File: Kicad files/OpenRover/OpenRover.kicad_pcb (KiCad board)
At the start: 2 copper layers, 0 parts

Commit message: Updated with Allan his work.
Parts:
- added D1: BAV23, Package_TO_SOT_SMD:SOT-23, F.Cu at (128.0, 64.0)
- added D2: BAV23, Package_TO_SOT_SMD:SOT-23, F.Cu at (139.0, 71.0)
- added D3: BAV23, Package_TO_SOT_SMD:SOT-23, F.Cu at (130.0, 56.0)
- added D4: BAV23, Package_TO_SOT_SMD:SOT-23, F.Cu at (135.0, 56.0)
- added D5: BAV23, Package_TO_SOT_SMD:SOT-23, F.Cu at (135.0, 62.0)
- added D6: BAV23, Package_TO_SOT_SMD:SOT-23, F.Cu at (134.0, 68.0)
- added D7: BAV23, Package_TO_SOT_SMD:SOT-23, F.Cu at (134.0, 74.0)
- added D8: 1N4148W, Diode_SMD:D_SOD-123, F.Cu at (157.0, 76.0)
- added D9: 1N4148W, Diode_SMD:D_SOD-123, F.Cu at (157.0, 71.0)
- added Q1: FQT7N10L, Package_TO_SOT_SMD:SOT-23, F.Cu at (143.0, 58.0)
- added Q2: BC846, Package_TO_SOT_SMD:SOT-23, F.Cu at (128.0, 70.0)
- added Q3: MMDT3906, Package_TO_SOT_SMD:SOT-363_SC-70-6, F.Cu at (127.0, 75.0)
- added U2: MAX4162, Package_TO_SOT_SMD:SOT-23-5, F.Cu at (149.0, 59.0)
- added U4: MAX6008AEUR+T, Package_TO_SOT_SMD:SOT-23, F.Cu at (147.0, 65.0)
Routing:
- net GND: track 0.00 -> 53.6 mm
- net Net-(C4-Pad2): track 0.00 -> 23.5 mm
- net Net-(C2-Pad2): track 0.00 -> 13.1 mm
- net Net-(Q2-Pad1): track 0.00 -> 6.59 mm
- net Net-(C6-Pad2): track 0.00 -> 5.79 mm
- net Net-(R6-Pad2): track 0.00 -> 4.85 mm
- net Net-(C10-Pad2): track 0.00 -> 4.51 mm
- net Net-(C12-Pad2): track 0.00 -> 4.10 mm
- net Net-(C10-Pad1): track 0.00 -> 4.10 mm
- net Net-(Q3-Pad1): track 0.00 -> 2.85 mm
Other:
- board outline added: 54.4 x 34.1 mm

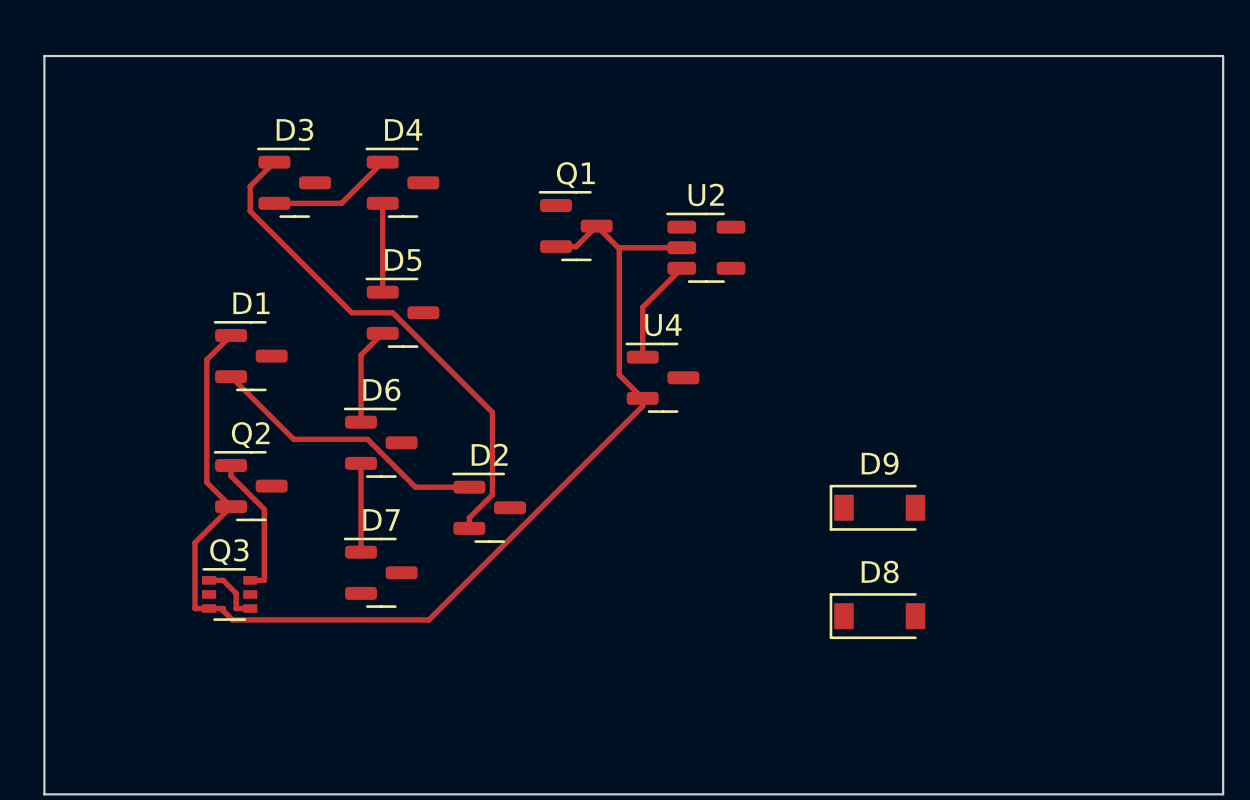
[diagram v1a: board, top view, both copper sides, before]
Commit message: Tested 74HC14 adding to the footprints
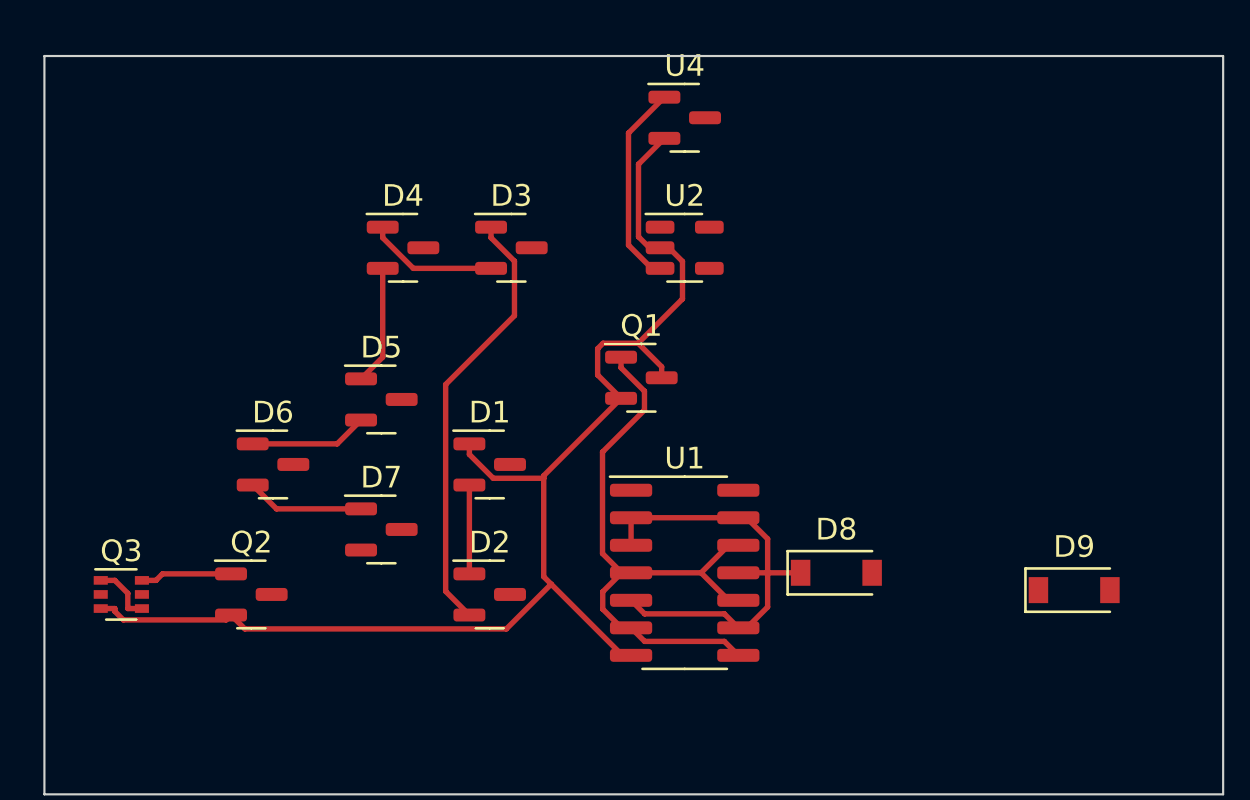
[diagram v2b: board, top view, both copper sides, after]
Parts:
- added U1: 74HC14, Package_SO:SOIC-14_3.9x8.7mm_P1.27mm, F.Cu at (148.0, 74.0)
- moved D1 12.1 mm to (139.0, 69.0)
- moved U4 12.0 mm to (148.0, 53.0)
- moved D3 10.4 mm to (140.0, 59.0)
- moved D9 9.75 mm to (166.0, 74.8)
- moved Q1 7.62 mm to (146.0, 65.0)
- moved D6 5.10 mm to (129.0, 69.0)
- moved Q2 5.00 mm to (128.0, 75.0)
- moved Q3 5.00 mm to (122.0, 75.0)
- moved D5 4.12 mm to (134.0, 66.0)
- moved D2 4.00 mm to (139.0, 75.0)
- moved D4 3.00 mm to (135.0, 59.0)
- moved D8 2.83 mm to (155.0, 74.0)
- moved D7 2.00 mm to (134.0, 72.0)
- moved U2 1.00 mm to (148.0, 59.0)
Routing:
- net Net-(Q1-Pad1): track 0.00 -> 28.9 mm
- net Net-(D8-Pad1): track 0.00 -> 21.2 mm
- net Net-(C2-Pad2): track 13.1 -> 4.10 mm
- net GND: track 53.6 -> 60.8 mm
- net Net-(R6-Pad2): track 4.85 -> 9.42 mm
- net Net-(C4-Pad2): track 23.5 -> 20.1 mm
- net Net-(Q2-Pad1): track 6.59 -> 4.24 mm
- net Net-(C10-Pad1): track 4.10 -> 5.51 mm
- net Net-(C12-Pad2): track 4.10 -> 5.46 mm
- net Net-(C10-Pad2): track 4.51 -> 5.46 mm

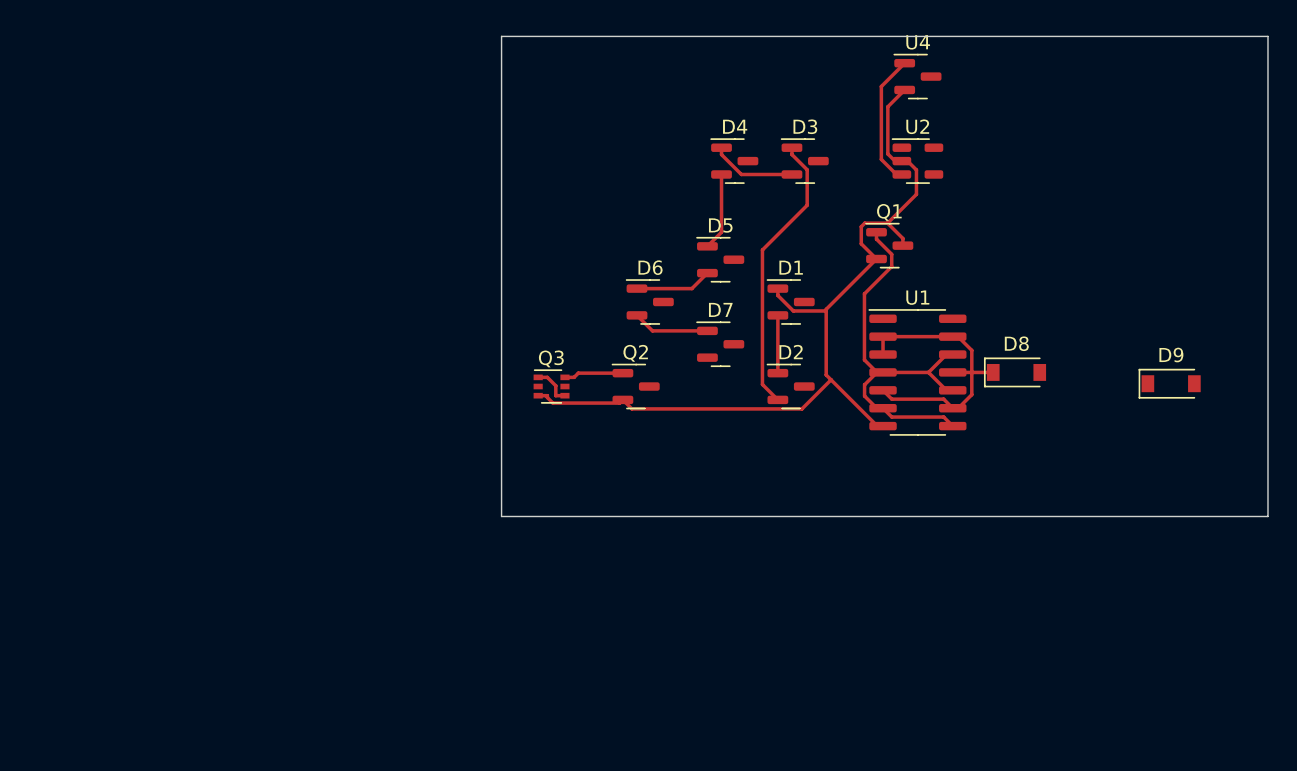
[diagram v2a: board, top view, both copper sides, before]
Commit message: Updated test for board sizes
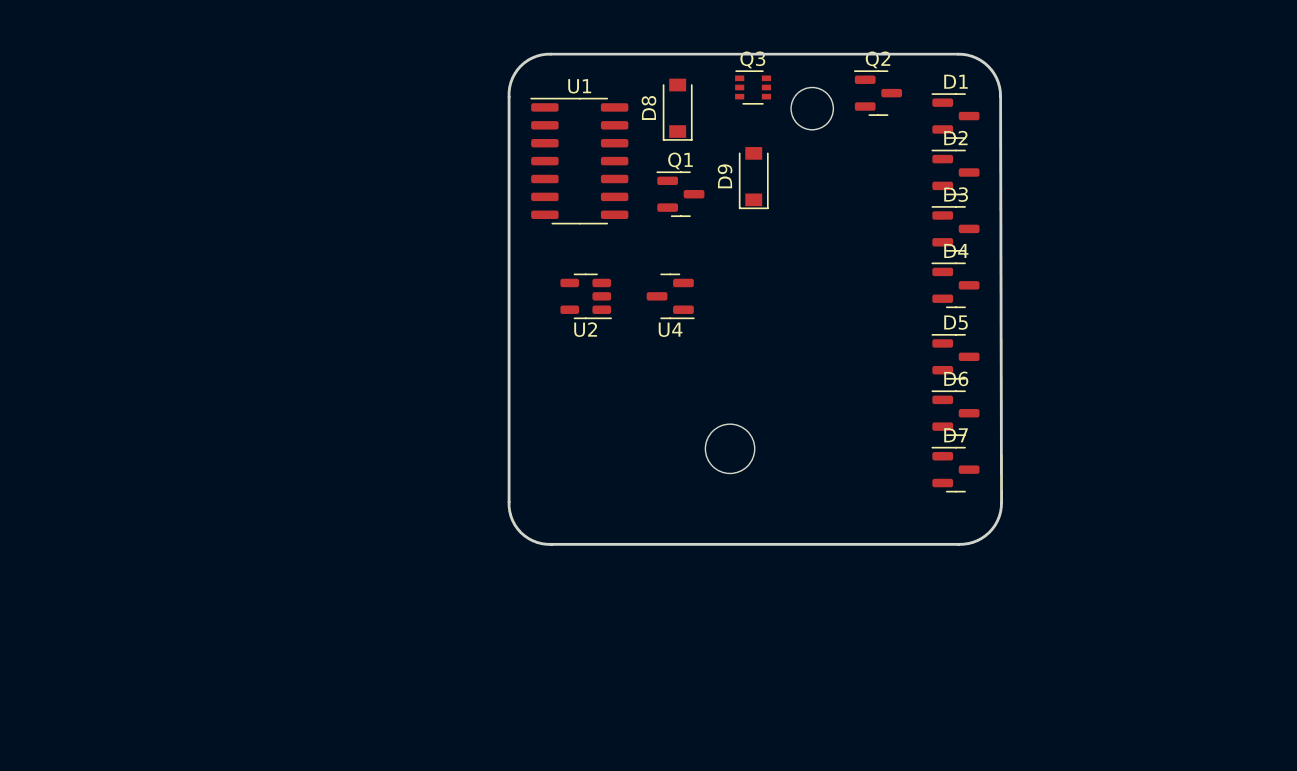
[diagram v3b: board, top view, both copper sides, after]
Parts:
- moved D9 33.1 mm to (136.3, 60.1), turned to 90 degrees
- moved D8 30.5 mm to (130.9, 55.2), turned to 90 degrees
- moved U1 28.3 mm to (124.0, 59.0)
- moved Q2 27.0 mm to (145.2, 54.2)
- moved Q3 25.6 mm to (136.3, 53.8)
- moved U2 25.5 mm to (124.4, 68.6), turned to 180 degrees
- moved U4 23.5 mm to (130.4, 68.6), turned to 180 degrees
- moved D6 23.1 mm to (150.7, 76.9)
- moved D2 19.2 mm to (150.7, 59.8)
- moved D7 18.9 mm to (150.7, 80.9)
- moved D5 18.1 mm to (150.7, 72.9)
- moved D4 18.0 mm to (150.7, 67.8)
- moved D1 17.6 mm to (150.7, 55.8)
- moved Q1 15.3 mm to (131.2, 61.4)
- moved D3 11.7 mm to (150.7, 63.8)
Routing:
- net GND: track 60.8 -> 0.00 mm
- net Net-(Q1-Pad1): track 28.9 -> 0.00 mm
- net Net-(D8-Pad1): track 21.2 -> 0.00 mm
- net Net-(C4-Pad2): track 20.1 -> 0.00 mm
- net Net-(R6-Pad2): track 9.42 -> 0.00 mm
- net Net-(C6-Pad2): track 6.07 -> 0.00 mm
- net Net-(C10-Pad1): track 5.51 -> 0.00 mm
- net Net-(C12-Pad2): track 5.46 -> 0.00 mm
- net Net-(C10-Pad2): track 5.46 -> 0.00 mm
- net Net-(Q2-Pad1): track 4.24 -> 0.00 mm
- net Net-(C2-Pad2): track 4.10 -> 0.00 mm
- net Net-(Q3-Pad1): track 2.85 -> 0.00 mm
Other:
- board size 54.4 x 34.1 mm -> 35 x 34.8 mm

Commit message: Updated the files from the allan zip files.
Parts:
- added C1: 0.1, Resistor_SMD:R_0805_2012Metric, F.Cu at (112.0, 65.0)
- added C10: 0.1, Resistor_SMD:R_0805_2012Metric, F.Cu at (127.0, 71.0)
- added C11: 0.1, Resistor_SMD:R_0805_2012Metric, F.Cu at (129.6, 65.0)
- added C12: 0.1, Resistor_SMD:R_0805_2012Metric, F.Cu at (130.6, 71.0)
- added C13: 0.1, Resistor_SMD:R_0805_2012Metric, F.Cu at (133.0, 65.0)
- added C14: 0.1, Capacitor_SMD:C_0805_2012Metric, F.Cu at (133.9, 85.5)
- added C15: 1uF, Capacitor_SMD:C_0805_2012Metric, F.Cu at (114.0, 80.0)
- added C16: 1nF, Capacitor_SMD:C_0805_2012Metric, F.Cu at (118.5, 93.5)
- added C17: 10uF, Capacitor_SMD:C_1210_3225Metric, F.Cu at (102.0, 79.5)
- added C18: 1uF, Capacitor_SMD:C_0805_2012Metric, F.Cu at (90.5, 78.0)
- added C19: 1uF, Capacitor_SMD:C_0805_2012Metric, F.Cu at (127.5, 86.5)
- added C2: 0.1, Resistor_SMD:R_0805_2012Metric, F.Cu at (113.0, 71.0)
- added C20: C, Capacitor_SMD:C_0805_2012Metric, F.Cu at (145.5, 88.5)
- added C21: C, Capacitor_SMD:C_0805_2012Metric, F.Cu at (134.0, 82.0)
- added C22: C, Capacitor_SMD:C_0805_2012Metric, F.Cu at (134.5, 94.5)
- added C3: 0.1, Resistor_SMD:R_0805_2012Metric, F.Cu at (115.5, 65.0)
- added C4: 0.1, Resistor_SMD:R_0805_2012Metric, F.Cu at (116.6, 71.0)
- added C5: 0.1, Resistor_SMD:R_0805_2012Metric, F.Cu at (119.0, 65.0)
- added C6: 0.1, Resistor_SMD:R_0805_2012Metric, F.Cu at (120.0, 71.0)
- added C7: 0.1, Resistor_SMD:R_0805_2012Metric, F.Cu at (122.5, 65.0)
- added C8: 0.1, Resistor_SMD:R_0805_2012Metric, F.Cu at (123.5, 71.0)
- added C9: 0.1, Resistor_SMD:R_0805_2012Metric, F.Cu at (126.0, 65.0)
- added FB1: Ferrite_Bead, Resistor_SMD:R_0805_2012Metric, F.Cu at (86.5, 84.0)
- added FB2: Ferrite_Bead, Resistor_SMD:R_0805_2012Metric, F.Cu at (96.1, 68.0)
- added J1: Conn_01x03_Male, Connector_PinHeader_2.54mm:PinHeader_1x03_P2.54mm_Vertical, F.Cu at (102.0, 86.0)
- added L1: 2.2uH, Inductor_SMD:L_Taiyo-Yuden_MD-4040, F.Cu at (102.5, 66.5)
- added R1: 22M, Resistor_SMD:R_0805_2012Metric, F.Cu at (111.5, 75.0)
- added R10: R, Resistor_SMD:R_0805_2012Metric, F.Cu at (110.5, 80.0)
- added R11: 121k, Resistor_SMD:R_0805_2012Metric, F.Cu at (122.5, 89.0)
- added R12: 33k, Resistor_SMD:R_0805_2012Metric, F.Cu at (154.3, 91.4)
- added R13: 100, Resistor_SMD:R_0805_2012Metric, F.Cu at (127.6, 84.0)
- added R14: 100k, Resistor_SMD:R_0805_2012Metric, F.Cu at (133.0, 91.0)
- added R15: 1M49, Resistor_SMD:R_0805_2012Metric, F.Cu at (122.5, 86.0)
- added R16: 392k, Resistor_SMD:R_0805_2012Metric, F.Cu at (145.4, 79.0)
- added R17: 1M, Resistor_SMD:R_0805_2012Metric, F.Cu at (125.0, 94.5)
- added R18: 499k, Resistor_SMD:R_0805_2012Metric, F.Cu at (133.5, 98.5)
- added R19: 1k, Resistor_SMD:R_0805_2012Metric, F.Cu at (154.4, 85.5)
- added R2: 22M, Resistor_SMD:R_0805_2012Metric, F.Cu at (116.4, 75.0)
- added R20: 100k, Resistor_SMD:R_0805_2012Metric, F.Cu at (154.3, 88.5)
- added R21: 47k, Resistor_SMD:R_0805_2012Metric, F.Cu at (158.8, 85.5)
- added R22: 20k, Resistor_SMD:R_0805_2012Metric, F.Cu at (141.5, 99.5)
- added R3: 22M, Resistor_SMD:R_0805_2012Metric, F.Cu at (121.0, 75.0)
- added R4: 22M, Resistor_SMD:R_0805_2012Metric, F.Cu at (125.4, 75.0)
- added R5: 3.16M, Resistor_SMD:R_0805_2012Metric, F.Cu at (158.7, 94.4)
- added R6: 560K, Resistor_SMD:R_0805_2012Metric, F.Cu at (158.7, 91.4)
- added R7: 4M7, Resistor_SMD:R_1206_3216Metric, F.Cu at (134.0, 73.0)
- added R8: 100K, Resistor_SMD:R_0805_2012Metric, F.Cu at (130.0, 79.5)
- added R9: 100K, Resistor_SMD:R_0805_2012Metric, F.Cu at (158.8, 88.4)
- added U3: CD14538BM, Package_SO:SOIC-16_3.9x9.9mm_P1.27mm, F.Cu at (109.5, 95.5)
- Q1: value FQT7N10L -> FQT7N10; footprint Package_TO_SOT_SMD:SOT-23 -> Package_TO_SOT_SMD:SOT-223-3_TabPin2
- moved D8 44.3 mm to (96.0, 82.5), turned to 0 degrees
- moved Q2 43.6 mm to (128.5, 94.5)
- moved Q3 41.9 mm to (132.5, 95.5)
- moved D9 41.4 mm to (118.5, 97.5), turned to 0 degrees
- moved D1 39.6 mm to (113.0, 68.0), turned to 90 degrees
- moved D2 35.2 mm to (116.5, 68.0), turned to 90 degrees
- moved D3 31.0 mm to (120.0, 67.9), turned to 90 degrees
- moved U1 30.9 mm to (109.0, 86.0), turned to 90 degrees
- moved Q1 28.9 mm to (104.5, 72.5)
- moved D4 27.2 mm to (123.5, 68.0), turned to 90 degrees
- moved D5 24.2 mm to (127.0, 68.0), turned to 90 degrees
- moved D6 22.1 mm to (130.5, 68.0), turned to 90 degrees
- moved D7 21.1 mm to (134.0, 68.0), turned to 90 degrees
- moved U4 15.5 mm to (120.5, 80.5)
- moved U2 11.9 mm to (125.5, 80.5), turned to 0 degrees
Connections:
- net Net-(R6-Pad2) renamed +2V5
- D1 pad 1: GND -> Net-(C2-Pad1)
- Q1 pad 1: Net-(Q1-Pad1) -> Net-(C2-Pad1)
- Q1 pad 2: GND -> Net-(Q1-Pad2)
- U1 pad 10: Net-(Q1-Pad1) -> Net-(Q1-Pad2)
- U1 pad 12: Net-(Q1-Pad1) -> Net-(Q1-Pad2)
- U1 pad 4: Net-(Q1-Pad1) -> Net-(Q1-Pad2)
- U1 pad 6: Net-(Q1-Pad1) -> Net-(Q1-Pad2)
- U1 pad 8: Net-(Q1-Pad1) -> Net-(Q1-Pad2)
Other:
- board size 35 x 34.8 mm -> 36 x 36 mm

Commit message: quick  test parts layout/route and 3d models
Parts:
- moved R5 41.0 mm to (120.1, 80.5), turned to -90 degrees
- moved R20 34.5 mm to (120.3, 94.5), turned to 90 degrees
- moved R12 31.2 mm to (123.3, 94.5), turned to 90 degrees
- moved R21 30.4 mm to (130.1, 95.7), turned to 180 degrees
- moved R6 29.9 mm to (128.9, 92.5)
- moved R9 29.9 mm to (128.9, 89.5)
- moved FB1 26.5 mm to (108.4, 69.0)
- moved R19 25.7 mm to (128.7, 86.4)
- moved D8 22.5 mm to (117.2, 90.0)
- moved C20 21.5 mm to (126.3, 98.1)
- moved C18 19.9 mm to (106.3, 65.8), turned to 90 degrees
- moved R16 17.4 mm to (128.7, 83.8)
- moved FB2 13.6 mm to (106.2, 77.1)
- moved R22 11.6 mm to (130.0, 98.2)
- moved Q3 10.2 mm to (122.6, 97.8), turned to 90 degrees
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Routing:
- net GND: track 0.00 -> 187.2 mm, vias 0 -> 2
- net +3V3: track 0.00 -> 93.1 mm, vias 0 -> 2
- net Net-(C14-Pad1): track 0.00 -> 43.9 mm, vias 0 -> 4
- net Net-(C19-Pad1): track 0.00 -> 41.1 mm
- net Net-(Q1-Pad2): track 0.00 -> 36.3 mm
- net Net-(R8-Pad2): track 0.00 -> 33.5 mm
- net Net-(C20-Pad1): track 0.00 -> 29.5 mm, vias 0 -> 2
- net Net-(D9-Pad2): track 0.00 -> 27.1 mm, vias 0 -> 2
- net Net-(C21-Pad1): track 0.00 -> 26.3 mm
- net Net-(D8-Pad1): track 0.00 -> 24.1 mm
- net +2V5: track 0.00 -> 22.5 mm, vias 0 -> 2
- net Net-(C2-Pad1): track 0.00 -> 21.9 mm
- net Net-(C16-Pad1): track 0.00 -> 21.5 mm
- net Net-(D9-Pad1): track 0.00 -> 18.6 mm, vias 0 -> 2
- net Net-(Q2-Pad1): track 0.00 -> 18.0 mm
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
